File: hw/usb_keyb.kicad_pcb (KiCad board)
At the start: 2 copper layers, 99.1 x 48.3 mm, 105 parts, among them J10 SPI, J11 RMII, J12 PS2, J2 Micro_SD_Card, J3 USB_1, J4 ZX-BUS, J5 MX_ROW, J6 MX_COL, J7 I2C, J8 UART, J9 PROG, SW1 RESET, SW2 OUTPUT, SW3 MATRIX, U1 LM3671MF, U2 STM32F407VETx, U3 STMPS2161STR, U5 74LS245, Y1 8MHz

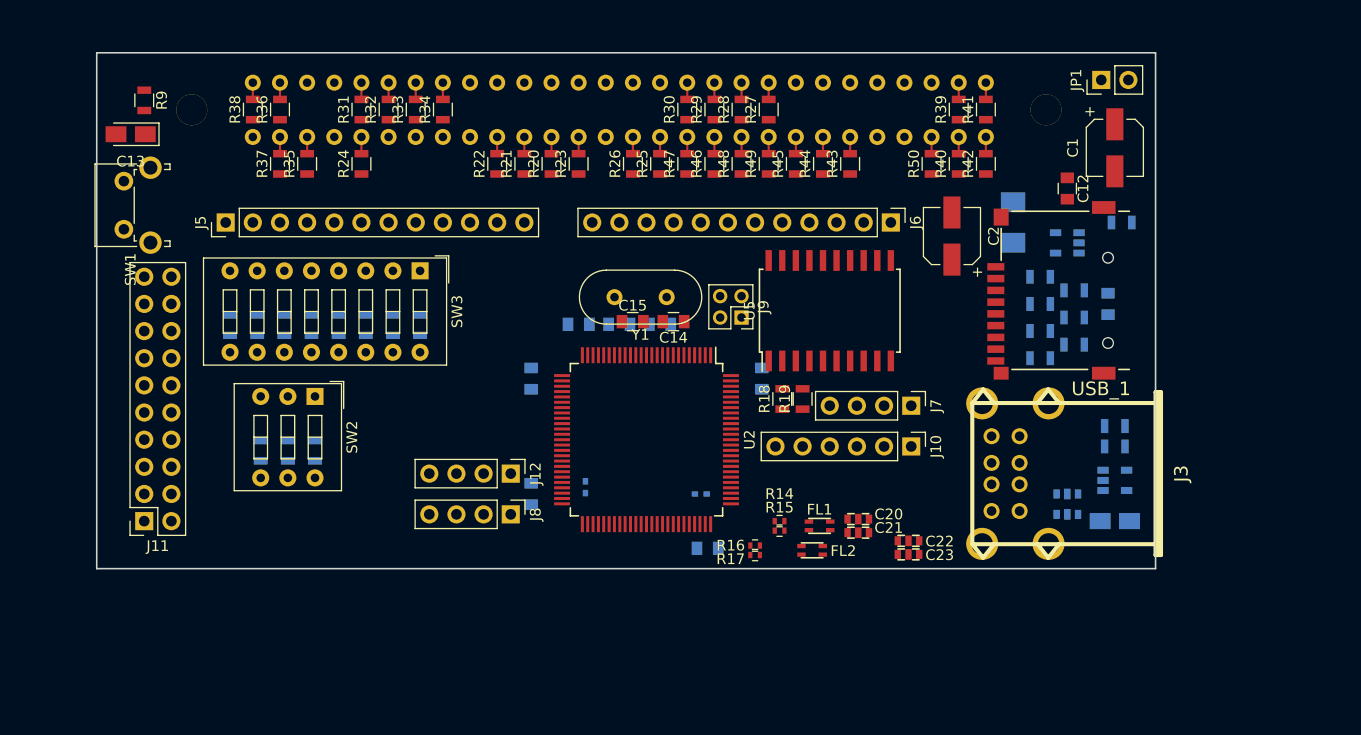
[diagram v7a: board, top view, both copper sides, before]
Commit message: Обновлена схема защиты USB
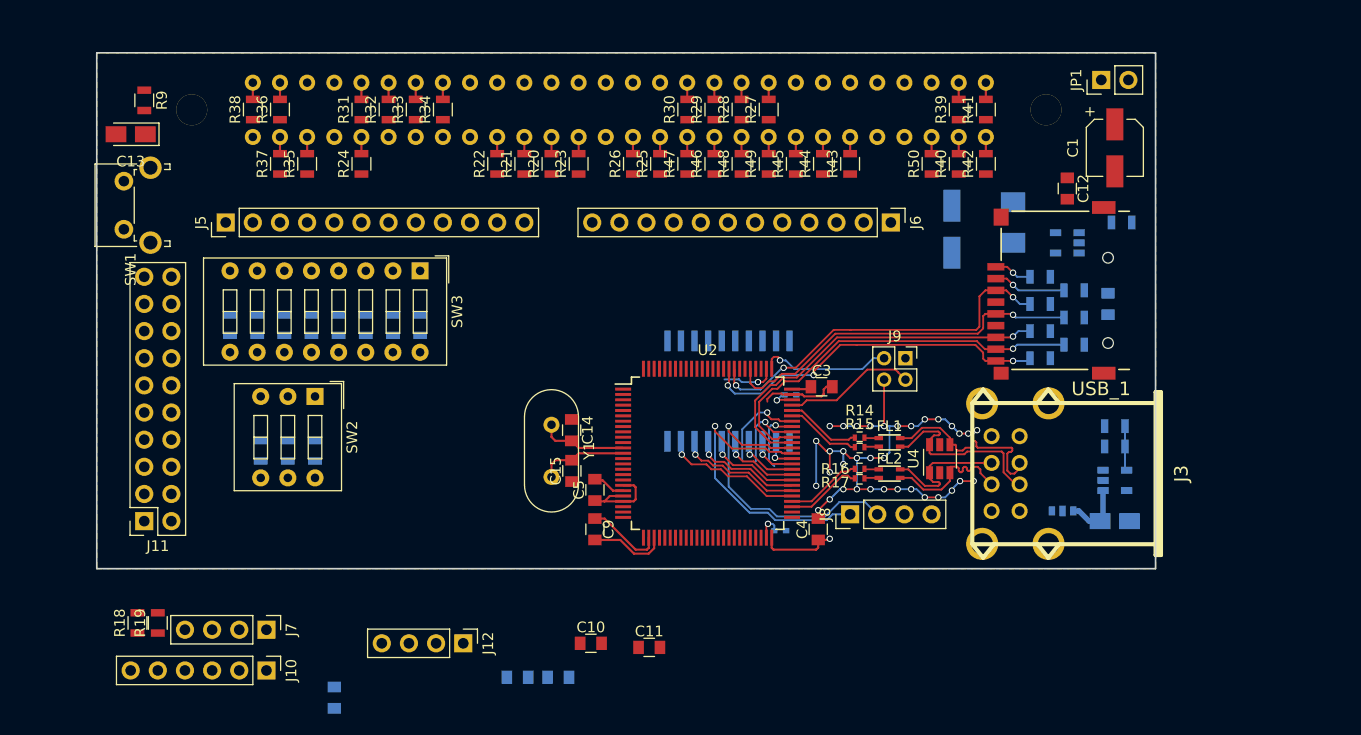
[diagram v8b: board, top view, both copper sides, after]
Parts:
- removed C20, C21, C22, C23, C24: NFM21PC104R1E3D, Projects:NFM21P
- added C10: 100n, Capacitors_SMD:C_0805, F.Cu at (142.7, 115.6)
- added C11: 100n, Capacitors_SMD:C_0805, F.Cu at (148.2, 116.0)
- added U4: NUP4201MR6, TO_SOT_Packages_SMD:TSOT-23-6, F.Cu at (175.4, 98.3)
- C2, U5: moved to B.Cu
- C3, C4, C5, C9: moved to F.Cu
- moved R18 63.9 mm to (100.3, 113.7)
- moved R19 63.9 mm to (102.2, 113.7)
- moved J10 63.9 mm to (112.4, 118.1)
- moved J7 63.9 mm to (112.4, 114.3)
- moved C6 34.4 mm to (139.7, 118.7)
- moved C7 34.4 mm to (135.9, 118.7)
- moved J8 31.8 mm to (167.0, 103.5), turned to 90 degrees
- moved C3 27.2 mm to (164.3, 91.6), turned to 0 degrees
- moved C8 26.5 mm to (118.7, 120.7)
- moved C9 21.0 mm to (143.1, 104.9), turned to 90 degrees
- moved C19 18.7 mm to (160.5, 105.0), turned to 0 degrees
- moved J12 16.5 mm to (130.8, 115.6)
- moved Y1 16.1 mm to (139.1, 95.1), turned to 270 degrees
- moved J9 15.8 mm to (172.2, 88.9), turned to 0 degrees
- moved C5 15.6 mm to (143.1, 101.2), turned to 90 degrees
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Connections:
- FL1 pad 2: Net-(C20-Pad1) -> F2_P
- FL1 pad 4: Net-(C21-Pad1) -> F2_N
- FL2 pad 2: Net-(C22-Pad1) -> H2_P
- FL2 pad 4: Net-(C23-Pad1) -> H2_N
- J3 pad 1: Net-(C24-Pad3) -> Net-(C17-Pad1)
- J3 pad 5: Net-(C25-Pad3) -> Net-(C17-Pad1)
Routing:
- net GND: track 0.00 -> 74.4 mm, vias 0 -> 35
- net SD1: track 0.00 -> 37.2 mm, vias 0 -> 1
- net CMD: track 0.00 -> 35.3 mm, vias 0 -> 3
- net SD0: track 0.00 -> 34.9 mm, vias 0 -> 1
- net CK: track 0.00 -> 34.6 mm, vias 0 -> 1
- net CD: track 0.00 -> 33.4 mm, vias 0 -> 3
- net UART_RX: track 0.00 -> 28.8 mm, vias 0 -> 1
- net UART_TX: track 0.00 -> 28.6 mm, vias 0 -> 1
- net +3V3: track 0.00 -> 24.7 mm, vias 0 -> 1
- net F2_P: track 0.00 -> 17.8 mm
- net F2_N: track 0.00 -> 17.8 mm
- net D0: track 0.00 -> 13.2 mm, vias 0 -> 1
- net H2_P: track 0.00 -> 12.7 mm
- net H2_N: track 0.00 -> 12.7 mm
- net SWCLK: track 0.00 -> 12.5 mm, vias 0 -> 1
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- added copper zone on In2.Cu, net +3V3
- added copper zone on B.Cu, net GND
- added copper zone on F.Cu, net GND
- added copper zone on In1.Cu, net GND
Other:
- copper layers 2 -> 4
- rule pad_to_mask_clearance: 0.2 -> 0.1
